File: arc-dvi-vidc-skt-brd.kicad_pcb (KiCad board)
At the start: 4 copper layers, 52.1 x 72 mm, 29 parts, among them IC1 SN74ALVC164245, IC2 SN74ALVC164245, IC3 SN74ALVC164245, J1 Connector_50pin_FFC, U1 MIC5219 3.3V

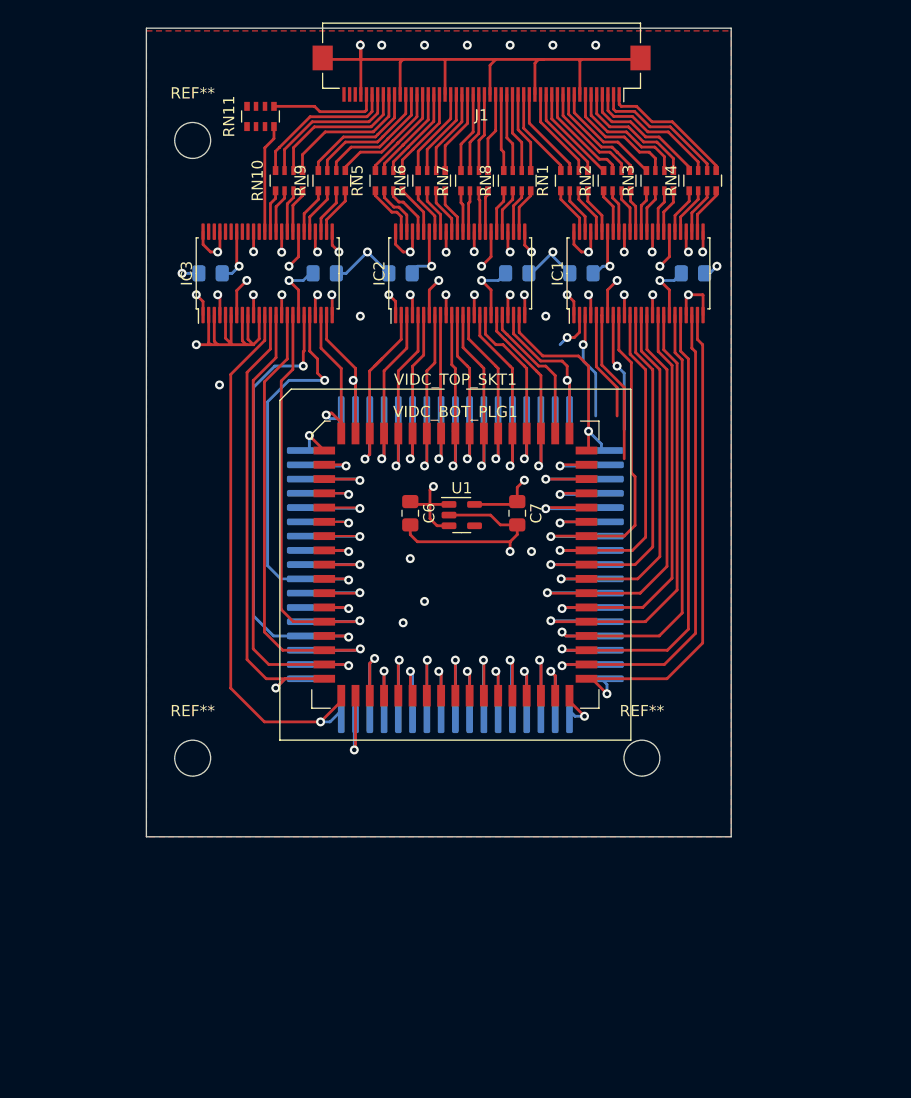
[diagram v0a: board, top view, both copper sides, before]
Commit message: Placed, partially routed
Same schematic as A3000 arc-dvi-vidc-brds, same FFC pinout (yay).
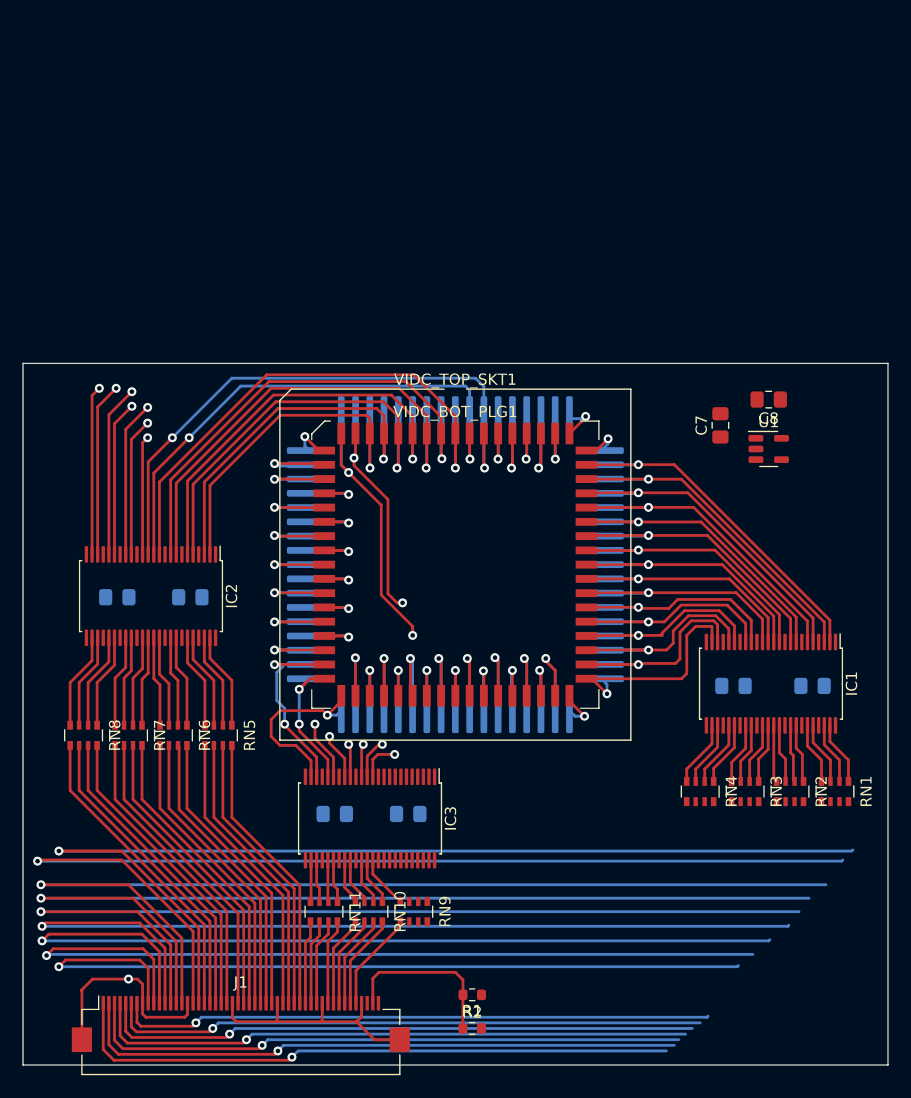
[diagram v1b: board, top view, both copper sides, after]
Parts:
- removed REF** (x3): MountingHole_3.2mm_M3, MountingHole:MountingHole_3.2mm_M3
- added R1: 4K7, Resistor_SMD:R_0603_1608Metric, F.Cu at (84.9, 141.1)
- added R2: 4K7, Resistor_SMD:R_0603_1608Metric, F.Cu at (84.9, 144.1)
- C6: moved to B.Cu
- C8: moved to F.Cu
- moved J1 87.3 mm to (64.3, 143.7), turned to 0 degrees
- moved RN11 71.0 mm to (71.7, 133.7), turned to -90 degrees
- moved RN9 65.5 mm to (79.7, 133.7), turned to -90 degrees
- moved RN10 65.5 mm to (75.7, 133.7), turned to -90 degrees
- moved RN8 62.7 mm to (50.3, 118.0), turned to -90 degrees
- moved RN1 59.1 mm to (117.2, 123.0), turned to -90 degrees
- moved RN7 58.2 mm to (54.3, 118.0), turned to -90 degrees
- moved RN2 56.5 mm to (113.2, 123.0), turned to -90 degrees
- moved RN3 54.9 mm to (109.2, 123.0), turned to -90 degrees
- moved RN6 54.5 mm to (58.3, 118.0), turned to -90 degrees
- moved RN4 54.4 mm to (105.2, 123.0), turned to -90 degrees
- moved RN5 51.7 mm to (62.3, 118.0), turned to -90 degrees
- moved IC3 49.4 mm to (75.8, 125.4), turned to -90 degrees
- moved C5 49.1 mm to (79.2, 125.0), turned to 180 degrees
- moved C2 48.5 mm to (72.7, 125.0)
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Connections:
- C7 pad 1: +3V3 -> +5V
- C8 pad 1: +5V -> +3V3
- IC3 pad 12: /NVIDW -> /SNDAK
- IC3 pad 13: /NVCS -> /VIDAK
- IC3 pad 14: /NHS -> /CKIN
- IC3 pad 16: /NSNDRQ -> /FLYBK
- IC3 pad 17: /FLYBK -> /NSNDRQ
- IC3 pad 20: /CKIN -> /NVCS
- IC3 pad 22: /SNDAK -> /NHS
- IC3 pad 23: /VIDAK -> /NVIDW
- IC3 pad 27: Net-(IC3-Pad27) -> Net-(RN11-Pad3)
- IC3 pad 30: Net-(IC3-Pad30) -> Net-(RN11-Pad1)
- J1 pad 38: Net-(J1-Pad38) -> Net-(RN11-Pad6)
- J1 pad 39: Net-(J1-Pad39) -> Net-(RN11-Pad7)
- J1 pad 41: Net-(J1-Pad41) -> Net-(RN11-Pad8)
- J1 pad 46: Net-(J1-Pad46) -> Net-(RN9-Pad5)
- J1 pad 49: unconnected-(J1-Pad49) -> /ID_DET
- RN11 pad 1: unconnected-(RN11-Pad1) -> Net-(RN11-Pad1)
- RN11 pad 2: unconnected-(RN11-Pad2) -> Net-(IC3-Pad29)
- RN11 pad 3: unconnected-(RN11-Pad3) -> Net-(RN11-Pad3)
- RN11 pad 4: Net-(IC3-Pad37) -> Net-(IC3-Pad26)
- RN11 pad 5: Net-(J1-Pad46) -> Net-(J1-Pad37)
- RN11 pad 6: unconnected-(RN11-Pad6) -> Net-(RN11-Pad6)
- RN11 pad 7: unconnected-(RN11-Pad7) -> Net-(RN11-Pad7)
- RN11 pad 8: unconnected-(RN11-Pad8) -> Net-(RN11-Pad8)
- RN9 pad 1: Net-(IC3-Pad30) -> unconnected-(RN9-Pad1)
- RN9 pad 2: Net-(IC3-Pad29) -> unconnected-(RN9-Pad2)
- RN9 pad 3: Net-(IC3-Pad27) -> unconnected-(RN9-Pad3)
- RN9 pad 4: Net-(IC3-Pad26) -> Net-(IC3-Pad37)
- RN9 pad 5: Net-(J1-Pad37) -> Net-(RN9-Pad5)
- RN9 pad 6: Net-(J1-Pad38) -> unconnected-(RN9-Pad6)
- RN9 pad 7: Net-(J1-Pad39) -> unconnected-(RN9-Pad7)
- RN9 pad 8: Net-(J1-Pad41) -> unconnected-(RN9-Pad8)
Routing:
- net GND: track 336.4 -> 89.3 mm, vias 55 -> 4
- net +5V: track 141.6 -> 8.34 mm, vias 8 -> 1
- net +3V3: track 104.9 -> 0.00 mm, vias 7 -> 0
- net Net-(J1-Pad17): track 8.27 -> 94.7 mm, vias 0 -> 1
- net Net-(J1-Pad18): track 8.14 -> 92.7 mm, vias 0 -> 1
- net Net-(J1-Pad15): track 8.19 -> 90.2 mm, vias 0 -> 1
- net Net-(J1-Pad14): track 8.31 -> 87.5 mm, vias 0 -> 1
- net Net-(J1-Pad13): track 8.69 -> 85.5 mm, vias 0 -> 1
- net Net-(J1-Pad12): track 9.21 -> 83.4 mm, vias 0 -> 1
- net Net-(J1-Pad11): track 9.49 -> 80.8 mm, vias 0 -> 1
- net Net-(J1-Pad10): track 9.62 -> 77.0 mm, vias 0 -> 1
- net Net-(J1-Pad9): track 10.2 -> 72.2 mm, vias 0 -> 1
- net /D18: track 12.9 -> 64.0 mm, vias 0 -> 2
- net /D16: track 21.3 -> 68.3 mm, vias 1 -> 2
- net /D17: track 17.2 -> 62.5 mm, vias 1 -> 2
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- removed copper zone on In2.Cu, net +3V3
- removed copper zone on In2.Cu, net +5V
- removed copper zone on F.Cu, net GND
- removed copper zone on In1.Cu, net GND
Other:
- board size 52.1 x 72 mm -> 77 x 62.5 mm
- board text removed: "And move regs -- so the stacked variant doesn't need to"
- board text removed: "IC3 needs to move right a bit :("

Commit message: Routed, passes DRC
Candidate!  V2
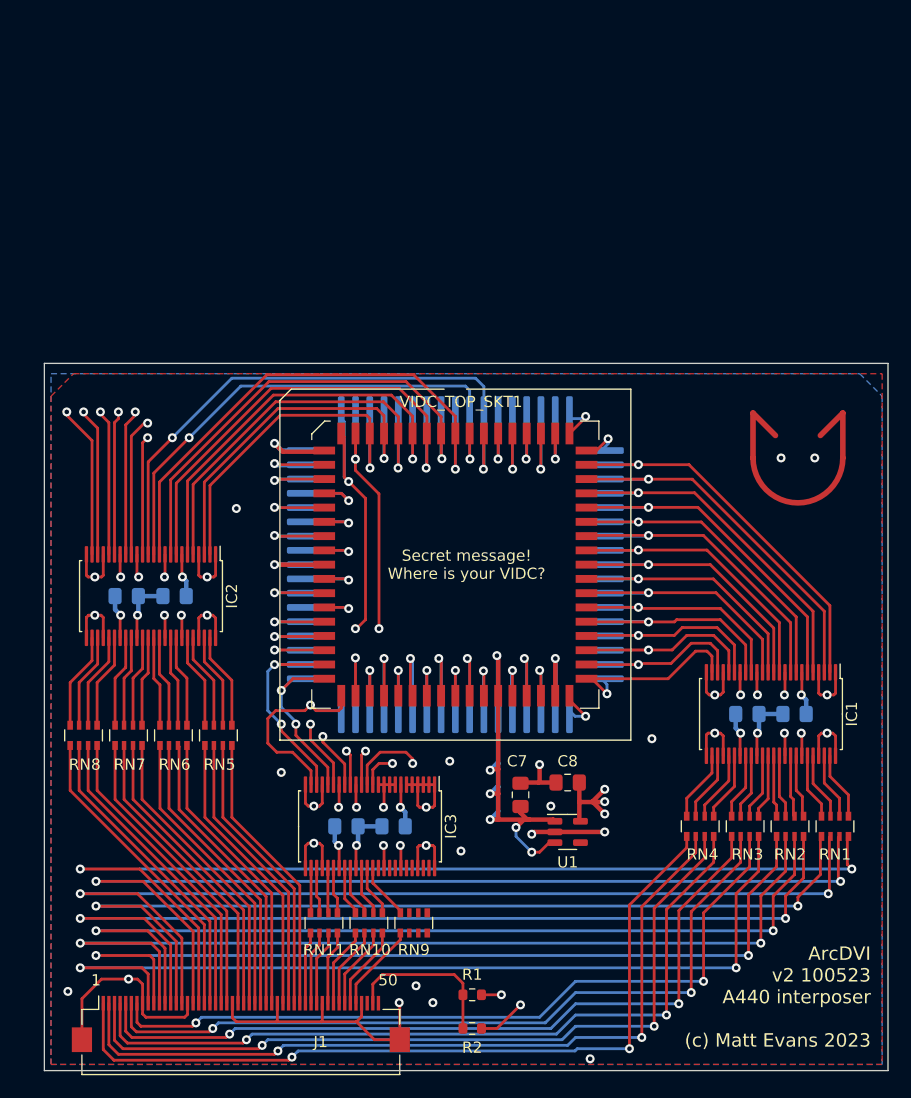
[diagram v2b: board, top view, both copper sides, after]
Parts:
- moved C8 38.5 mm to (93.4, 122.2)
- moved U1 38.5 mm to (93.4, 126.6)
- moved C7 37.4 mm to (89.2, 123.3)
- moved RN1 3.10 mm to (117.2, 126.1)
- moved RN2 3.10 mm to (113.2, 126.1)
- moved RN3 3.10 mm to (109.2, 126.1)
- moved RN4 3.10 mm to (105.2, 126.1)
- moved C6 2.97 mm to (113.6, 116.1)
- moved C3 2.79 mm to (109.4, 116.1), turned to 0 degrees
- moved IC1 2.70 mm to (111.5, 116.1)
- moved C5 1.70 mm to (77.9, 126.1)
- moved C2 1.51 mm to (73.7, 126.1), turned to 0 degrees
- moved C4 1.40 mm to (58.4, 105.6)
- moved RN10 1.00 mm to (75.7, 134.7)
- moved RN11 1.00 mm to (71.7, 134.7)
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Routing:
- net GND: track 89.3 -> 395.4 mm, vias 4 -> 45
- net +5V: track 8.34 -> 160.8 mm, vias 1 -> 12
- net +3V3: track 0.00 -> 142.3 mm, vias 0 -> 10
- net Net-(J1-Pad1): track 55.0 -> 72.8 mm, vias 1 -> 2
- net Net-(J1-Pad2): track 54.7 -> 72.0 mm, vias 1 -> 2
- net Net-(J1-Pad3): track 54.2 -> 71.3 mm, vias 1 -> 2
- net Net-(J1-Pad4): track 53.9 -> 70.5 mm, vias 1 -> 2
- net Net-(J1-Pad5): track 53.5 -> 70.1 mm, vias 1 -> 2
- net Net-(J1-Pad6): track 53.3 -> 69.3 mm, vias 1 -> 2
- net Net-(J1-Pad7): track 53.1 -> 68.6 mm, vias 1 -> 2
- net /VIDAK: track 37.7 -> 46.0 mm
- net Net-(J1-Pad9): track 72.2 -> 79.8 mm, vias 1 -> 2
- net Net-(J1-Pad17): track 94.7 -> 87.3 mm, vias 1 -> 2
- net /NVCS: track 12.8 -> 17.3 mm
- net /FLYBK: track 29.6 -> 25.4 mm
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- added copper zone on In2.Cu, net +3V3
- added copper zone on In2.Cu, net +5V
- added copper zone on B.Cu, net GND
- added copper zone on F.Cu, net GND
- added copper zone on In1.Cu, net GND
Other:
- board size 77 x 62.5 mm -> 75.1 x 63 mm
- board text added: "1"
- board text added: "50"
- board text added: "ArcDVI v2 100523 A440 interposer (c) Matt Evans 2023"
- board text added: "Secret message! Where is your VIDC?"

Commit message: Final tweaks for aesthetics
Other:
- board size 75.1 x 63 mm -> 73.6 x 63 mm
- board text added: "ArcDVI v2 110523 A440 interposer (c) Matt Evans 2023"
- board text removed: "ArcDVI v2 100523 A440 interposer (c) Matt Evans 2023"
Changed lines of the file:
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@@
     )
   )
-  (gr_line (start 117.89 93.27) (end 117.89 89.27) (layer "F.Cu") (width 0.5))
-  (gr_line (start 117.89 89.27) (end 115.89 91.27) (layer "F.Cu") (width 0.5))
-  (gr_line (start 109.89 93.27) (end 109.89 89.27) (layer "F.Cu") (width 0.5))
-  (gr_arc (start 117.89 93.27) (mid 113.89 97.27) (end 109.89 93.27) (layer "F.Cu") (width 0.5))
-  (gr_line (start 109.89 89.27) (end 111.89 91.27) (layer "F.Cu") (width 0.5))
-  (gr_rect (start 46.795 84.85) (end 121.91 147.82) (layer "Edge.Cuts") (width 0.1) (fill none))
+  (gr_line (start 116.39 92.77) (end 116.39 88.77) (layer "F.Cu") (width 0.5))
+  (gr_line (start 116.39 88.77) (end 114.39 90.77) (layer "F.Cu") (width 0.5))
+  (gr_line (start 108.39 92.77) (end 108.39 88.77) (layer "F.Cu") (width 0.5))
+  (gr_arc (start 116.39 92.77) (mid 112.39 96.77) (end 108.39 92.77) (layer "F.Cu") (width 0.5))
+  (gr_line (start 108.39 88.77) (end 110.39 90.77) (layer "F.Cu") (width 0.5))
+  (gr_rect (start 46.795 84.85) (end 120.41 147.82) (layer "Edge.Cuts") (width 0.1) (fill none))
+  (gr_text "ArcDVI\nv2 110523\nA440 interposer\n\n(c) Matt Evans 2023\n" (at 119.39 141.77) (layer "F.Cu")
+    (effects (font (size 1.2 1.1) (thickness 0.15)) (justify right))
+  )
   (gr_text "50" (at 77.39 139.77) (layer "F.SilkS")
     (effects (font (size 1 1) (thickness 0.15)))
@@
   (gr_text "Secret message!\nWhere is your VIDC?" (at 84.39 102.77) (layer "F.SilkS")
     (effects (font (size 1 1) (thickness 0.15)))
-  )
-  (gr_text "ArcDVI\nv2 100523\nA440 interposer\n\n(c) Matt Evans 2023\n" (at 120.39 141.27) (layer "F.SilkS")
-    (effects (font (size 1.2 1.2) (thickness 0.15)) (justify right))
   )
   (gr_text "1" (at 51.39 139.77) (layer "F.SilkS")
@@
   (via (at 61.29 107.27) (size 0.8) (drill 0.4) (layers "F.Cu" "B.Cu") (net 2))
   (via (at 89.19 141.97) (size 0.8) (drill 0.4) (layers "F.Cu" "B.Cu") (net 2))
-  (via (at 115.39 93.27) (size 0.8) (drill 0.4) (layers "F.Cu" "B.Cu") (net 2))
+  (via (at 113.89 92.77) (size 0.8) (drill 0.4) (layers "F.Cu" "B.Cu") (net 2))
   (via (at 106.49 114.37) (size 0.8) (drill 0.4) (layers "F.Cu" "B.Cu") (net 2))
   (via (at 61.29 103.87) (size 0.8) (drill 0.4) (layers "F.Cu" "B.Cu") (net 2))
@@
   (via (at 92.29 111.125) (size 0.8) (drill 0.4) (layers "F.Cu" "B.Cu") (net 2))
   (via (at 80.79 127.77) (size 0.8) (drill 0.4) (layers "F.Cu" "B.Cu") (net 2))
-  (via (at 112.39 93.27) (size 0.8) (drill 0.4) (layers "F.Cu" "B.Cu") (net 2))
+  (via (at 110.89 92.77) (size 0.8) (drill 0.4) (layers "F.Cu" "B.Cu") (net 2))
   (via (at 100.89 118.27) (size 0.8) (drill 0.4) (layers "F.Cu" "B.Cu") (net 2))
   (via (at 80.79 124.37) (size 0.8) (drill 0.4) (layers "F.Cu" "B.Cu") (net 2))
@@
   (segment (start 63.49 113.07) (end 63.49 117.07) (width 0.25) (layer "F.Cu") (net 67))
   (segment (start 61.54 111.12) (end 63.49 113.07) (width 0.25) (layer "F.Cu") (net 67))
-  (segment (start 69.99 115.77) (end 67.39 115.77) (width 0.25) (layer "F.Cu") (net 68))
   (segment (start 70.49 115.27) (end 70.99 115.77) (width 0.25) (layer "F.Cu") (net 68))
-  (segment (start 70.49 115.27) (end 69.99 115.77) (width 0.25) (layer "F.Cu") (net 68))
+  (segment (start 68.89 119.47) (end 70.54 121.12) (width 0.25) (layer "F.Cu") (net 68))
+  (segment (start 67.89 115.27) (end 66.69 116.47) (width 0.25) (layer "F.Cu") (net 68))
+  (segment (start 67.49 119.47) (end 68.89 119.47) (width 0.25) (layer "F.Cu") (net 68))
   (segment (start 70.54 121.12) (end 70.54 122.3575) (width 0.25) (layer "F.Cu") (net 68))
-  (segment (start 67.39 115.77) (end 66.69 116.47) (width 0.25) (layer "F.Cu") (net 68))
-  (segment (start 67.49 119.47) (end 68.89 119.47) (width 0.25) (layer "F.Cu") (net 68))
-  (segment (start 68.89 119.47) (end 70.54 121.12) (width 0.25) (layer "F.Cu") (net 68))
   (segment (start 70.99 115.77) (end 72.99 115.77) (width 0.25) (layer "F.Cu") (net 68))
+  (segment (start 70.49 115.27) (end 67.89 115.27) (width 0.25) (layer "F.Cu") (net 68))
   (segment (start 66.69 116.47) (end 66.69 118.67) (width 0.25) (layer "F.Cu") (net 68))
+  (segment (start 72.99 115.77) (end 73.23 115.53) (width 0.25) (layer "F.Cu") (net 68))
   (segment (start 66.69 118.67) (end 67.49 119.47) (width 0.25) (layer "F.Cu") (net 68))
-  (segment (start 72.99 115.77) (end 73.23 115.53) (width 0.25) (layer "F.Cu") (net 68))
   (segment (start 73.23 115.53) (end 73.23 114.4425) (width 0.25) (layer "F.Cu") (net 68))
   (via (at 70.49 115.27) (size 0.8) (drill 0.4) (layers "F.Cu" "B.Cu") (net 68))
@@
     (polygon
       (pts
-        (xy 121.39 147.27)
+        (xy 119.89 147.27)
         (xy 47.39 147.27)
         (xy 47.39 87.77)
         (xy 49.39 85.77)
-        (xy 121.39 85.77)
+        (xy 119.89 85.77)
       )
     )
@@
     (polygon
       (pts
-        (xy 121.39 147.27)
+        (xy 119.89 147.27)
         (xy 47.39 147.27)
         (xy 47.39 85.77)
-        (xy 121.39 85.77)
+        (xy 119.89 85.77)
       )
     )
@@
         (xy 115.59 109.67)
         (xy 115.59 115.67)
-        (xy 102.29 115.67)
-        (xy 97.09 120.87)
-        (xy 91.99 120.87)
-        (xy 91.99 126.57)
+        (xy 101.89 115.67)
+        (xy 97.09 120.37)
+        (xy 90.49 120.37)
+        (xy 90.49 126.57)
         (xy 86.79 126.57)
         (xy 85.99 125.77)
@@
     (polygon
       (pts
-        (xy 121.39 87.77)
-        (xy 121.39 147.27)
+        (xy 119.89 87.77)
+        (xy 119.89 147.27)
         (xy 47.39 147.27)
         (xy 47.39 85.77)

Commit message: Add logo, final silkscreen tweak
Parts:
- added G***: LOGO, LOGO, F.Cu at (98.5, 136.7)
